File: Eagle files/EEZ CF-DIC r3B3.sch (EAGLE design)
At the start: 238 parts, among them IC1 MC79L05, IC2 LP2951, IC3 VIPer35L, IC4 SI8233BB-D-IS1, IC5 LM5041B, IC6 IR11688STRPBF, IC7 TL072, IC8 TL103W, IC9 TL431, P1 T910W-50K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

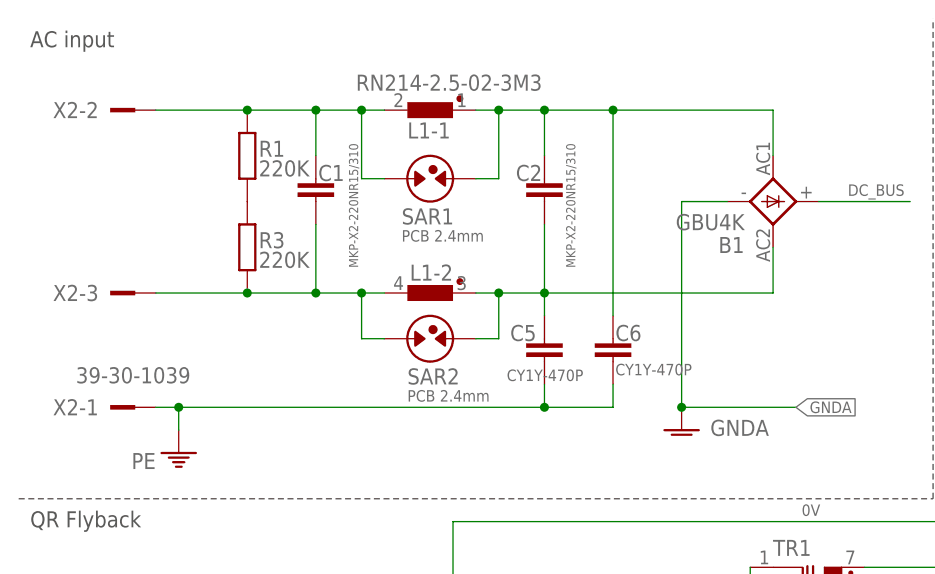
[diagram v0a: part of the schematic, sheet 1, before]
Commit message: Bridge rectifier relocated, Y2 capacitors optional positions added
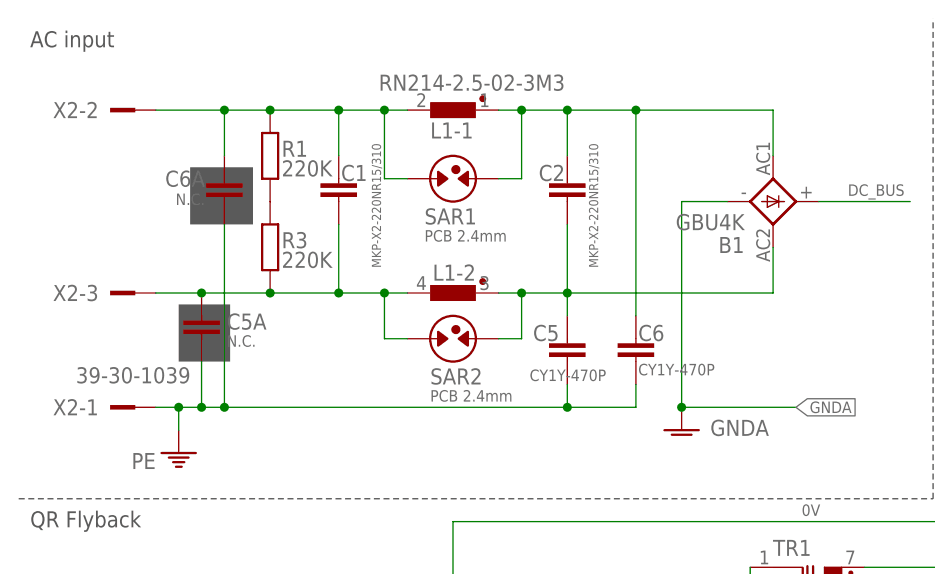
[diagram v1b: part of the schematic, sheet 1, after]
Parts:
- added C5A, C6A: N.C., EEZ_Lib1:C-EUCY
- C1, C2: device rcl:C-EU150-084X183 -> rcl:C-EU150-072X183
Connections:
- net N$28: now also C6A.2
- net N$30: now also C5A.2
- net PE: now also C5A.1, C6A.1
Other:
- moved on the sheet: C1, C2, C5, C6, L1-1, L1-2, R1, R3, SAR1, SAR2
